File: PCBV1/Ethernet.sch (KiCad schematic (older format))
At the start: 0 parts

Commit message: Added JTAG, USB OTG, USB Host, and Ethernet.
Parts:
- added C128, C130, C131, C133: 100n, Capacitor_SMD:C_0603_1608Metric, symbol Device:C
- added C129, C132: 22u, Capacitor_SMD:C_0603_1608Metric, symbol Device:C
- added C134: 2.2u, Capacitor_SMD:C_0603_1608Metric, symbol Device:C
- added FB6: 600R, Inductor_SMD:L_0603_1608Metric, symbol Device:Ferrite_Bead_Small
- added R46, R47, R50, R51, R53, R54, R55, R58, R59: 1k, Resistor_SMD:R_0603_1608Metric, symbol Device:R
- added R48: 6.49k, Resistor_SMD:R_0603_1608Metric, symbol Device:R
- added R49, R52, R56, R57, R60: 4.7k, Resistor_SMD:R_0603_1608Metric, symbol Device:R
- added U17: MCP112T-315E_LB, Personal_ICs:MCP112T-315E-LB, symbol Personal_ICs:MCP112T-315E_LB
- added U18: KSZ8081RNB, Personal_ICs:KSZ8081RNB, symbol Personal_ICs:KSZ8081RNB
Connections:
- new net: R48.2, U18.10 (REXT)
- new net: C133.2, C134.2, U18.2 (VDD_1.2)
- new net: C131.2, C132.2, FB6.1, U18.3 (VDDA_3.3)
- new net +3V3: C128.1, C129.1, C130.1, FB6.2, R46.1, R47.1, R49.1, R52.1, R56.1, R57.1, R60.1, U17.3 (VDD), U18.17 (VDDIO)
- new net CAST_OFF: R59.2, U18.19 (RXC/B-CAST_OFF)
- new net CONFIG0: R52.2, U18.28 (COL/CONFIG0)
- new net CONFIG1: R53.2, U18.29 (CRS/CONFIG1)
- new net ETH_RX_N: U18.4 (RXM)
- new net ETH_RX_P: U18.5 (RXP)
- new net ETH_TX_N: U18.6 (TXM)
- new net ETH_TX_P: U18.7 (TXP)
- new net GND: C128.2, C129.2, C130.2, C131.1, C132.1, C133.1, C134.1, R48.1, R50.1, R51.1, R53.1, R54.1, R55.1, R58.1, R59.1, U17.2 (VSS), U18.1 (GND_1), U18.33 (GND_2)
- new net LED0: R56.2, U18.30 (LED0/NWAYEN)
- new net LED1: R57.2, U18.31 (LED1/SPEED)
- new net MDC: R46.2, U18.12 (MDC)
- new net MDIO: R47.2, U18.11 (MDIO)
- new net NAND_TREE: R60.2, U18.21 (INTRP/NAND_TREE#)
- new net PHYAD0: R49.2, U18.13 (RXD3/PHYAD0)
- new net PHYAD1: R50.2, U18.14 (RXD2/PHYAD1)
- new net RCLK: U18.9 (XI)
- new net RXD0: R58.2, U18.16 (RXD0/DUPLEX)
- new net RXD1: R51.2, U18.15 (RXD1/PHYAD2)
- new net RXER: R55.2, U18.20 (RXER/ISO)
- new net RX_DV: R54.2, U18.18 (RXDV/CONFIG2)
- new net TXD0: U18.24 (TXD0)
- new net TXD1: U18.25 (TXD1)
- new net TXEN: U18.23 (TXEN)
- new net ~RESET: U17.1 (VOUT), U18.32 (RST#)
- no-connect marks 0 -> 4
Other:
- note added: "1%"
- note added: "Configuration strap resistors"
- note added: "Ethernet PHY"
- note added: "Voltage supervisor"

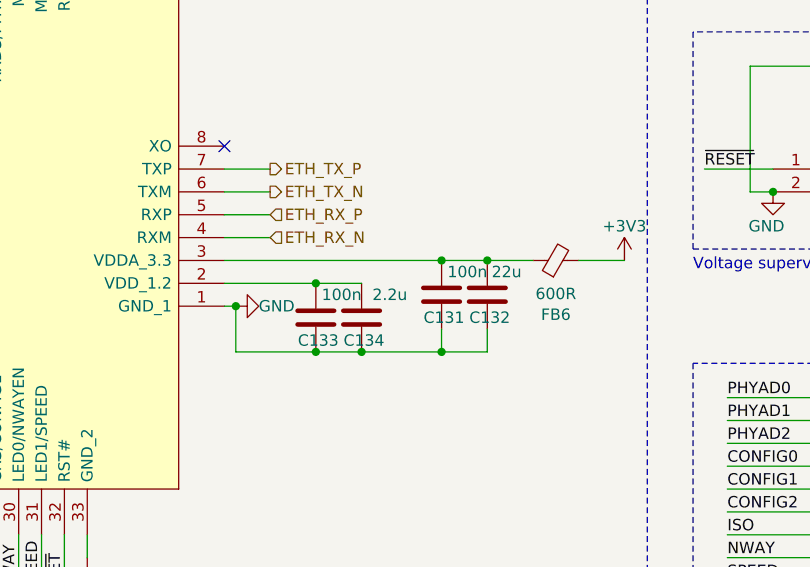
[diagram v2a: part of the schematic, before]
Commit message: Many changes to footprints (0603 -> 0402), basic DDR layout set, no traces made.
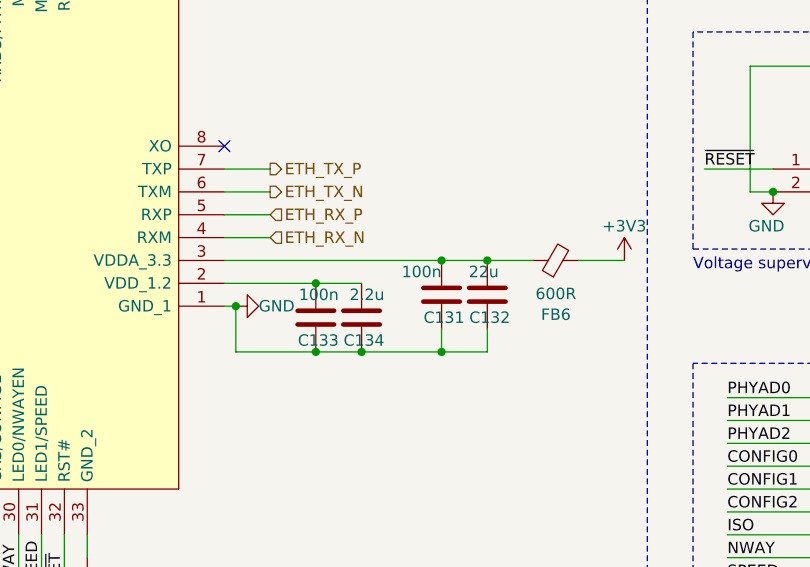
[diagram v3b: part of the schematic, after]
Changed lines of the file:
@@
 P 4100 3700
 F 0 "C133" H 4000 3800 50  0000 L CNN
-F 1 "100n" H 3900 3600 50  0000 L CNN
+F 1 "100n" H 4000 3600 50  0000 L CNN
 F 2 "Capacitor_SMD:C_0603_1608Metric" H 4138 3550 50  0001 C CNN
 F 3 "~" H 4100 3700 50  0001 C CNN
@@
 P 4300 3700
 F 0 "C134" H 4200 3800 50  0000 L CNN
-F 1 "2.2u" H 4100 3600 50  0000 L CNN
+F 1 "2.2u" H 4200 3600 50  0000 L CNN
 F 2 "Capacitor_SMD:C_0603_1608Metric" H 4338 3550 50  0001 C CNN
 F 3 "~" H 4300 3700 50  0001 C CNN
@@
 P 4650 3600
 F 0 "C131" H 4550 3700 50  0000 L CNN
-F 1 "100n" H 4450 3500 50  0000 L CNN
+F 1 "100n" H 4650 3500 50  0000 L CNN
 F 2 "Capacitor_SMD:C_0603_1608Metric" H 4688 3450 50  0001 C CNN
 F 3 "~" H 4650 3600 50  0001 C CNN
@@
 P 4850 3600
 F 0 "C132" H 4750 3700 50  0000 L CNN
-F 1 "22u" H 4700 3500 50  0000 L CNN
+F 1 "22u" H 4800 3500 50  0000 L CNN
 F 2 "Capacitor_SMD:C_0603_1608Metric" H 4888 3450 50  0001 C CNN
 F 3 "~" H 4850 3600 50  0001 C CNN
